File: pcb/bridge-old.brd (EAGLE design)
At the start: 104.2 x 63.6 mm, 38 parts, among them IC2 LM358D, IC3 78L05SMD, X1 PN61729-S

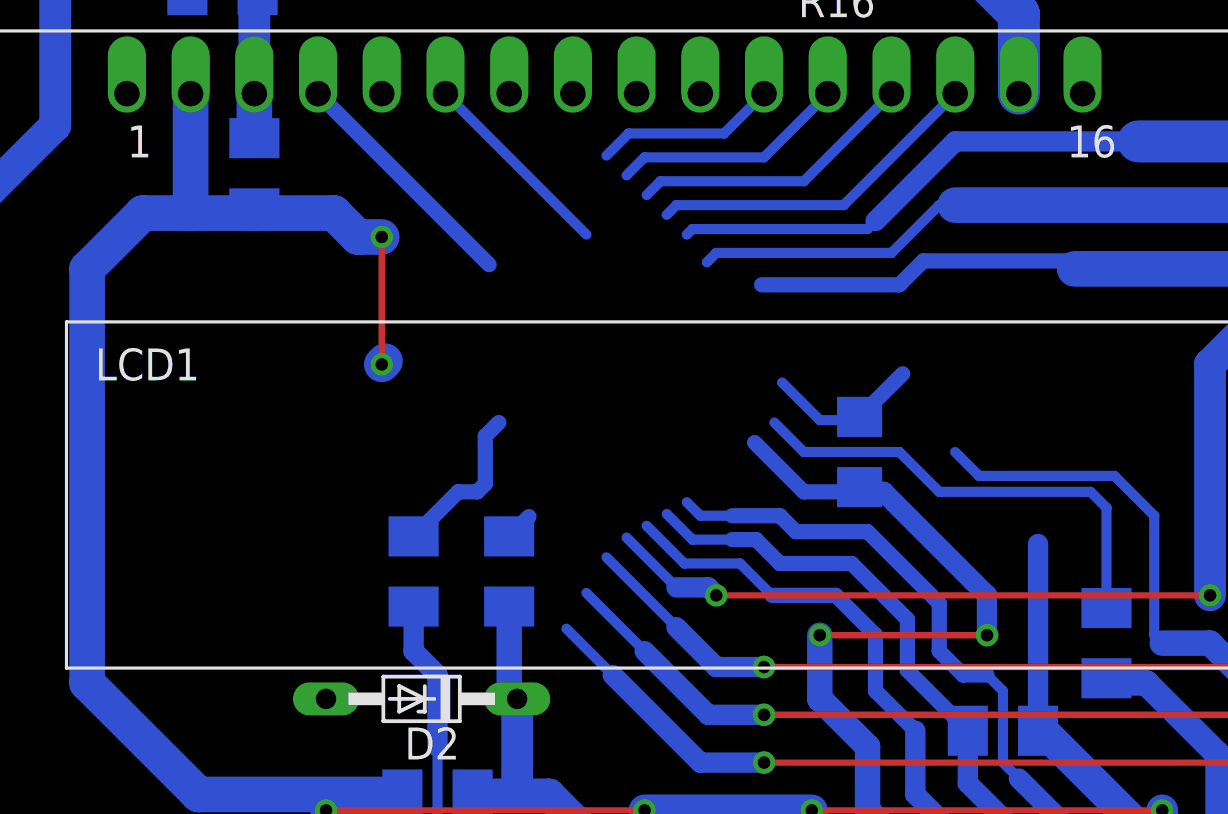
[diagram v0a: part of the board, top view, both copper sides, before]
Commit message: Rename 'bridge' project. Create board for new bridge.
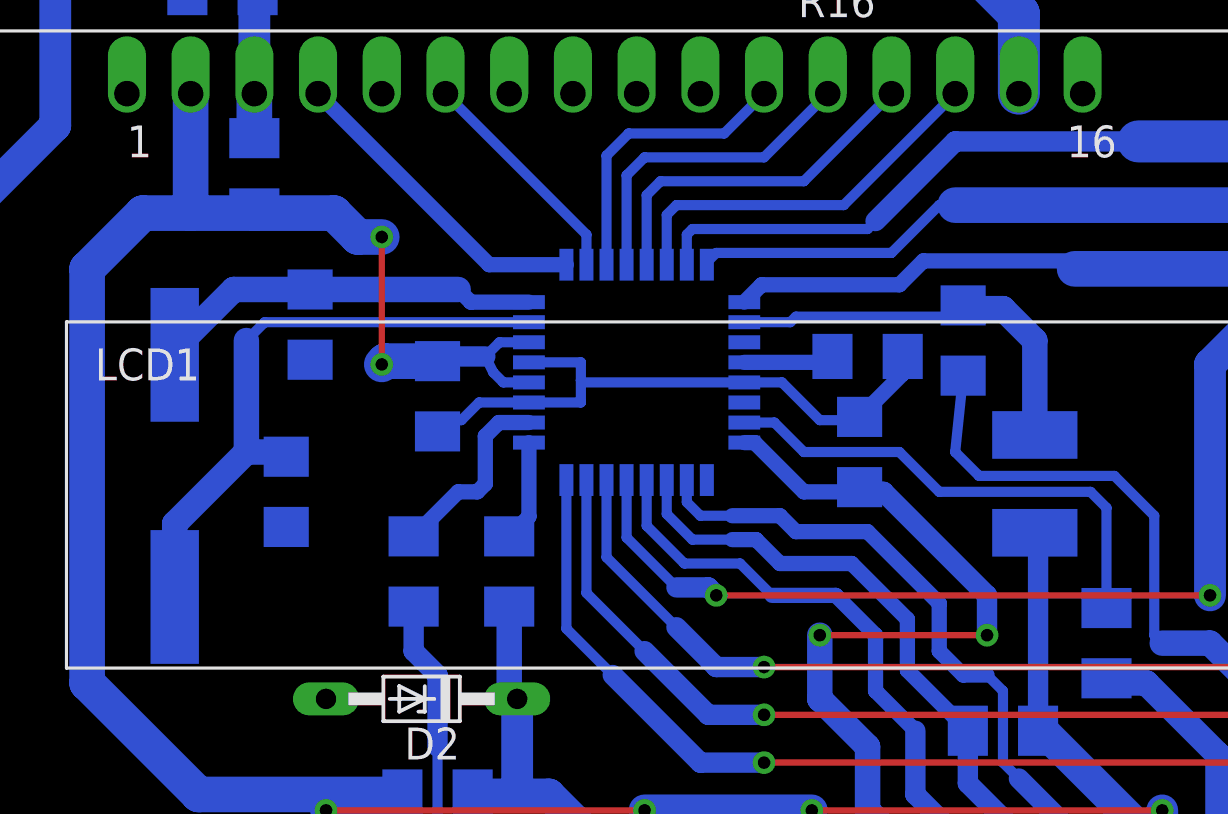
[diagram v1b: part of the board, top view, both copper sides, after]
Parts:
- added C1, C2: 22p, rcl:C1206
- added C3, C4, C5: 100n, rcl:C1206
- added IC1: MEGA8-AI, atmel:TQFP32-08
- added L1: 10u, rcl:L1812
- added Q1: 16MHz, crystal:HC49UP
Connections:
- new net N$10: C4.1, IC1.18, L1.2
- new net N$11: C1.1, IC1.8, Q1.1
- new net N$8: C3.1, IC1.20
- new net N$9: C2.1, IC1.7, Q1.2
- new net PC2: IC1.25
- new net PC6: IC1.19
- new net PC7: IC1.22
- net +5V: now also C5.1, IC1.4, IC1.6, L1.1
- net GND: now also C1.2, C2.2, C3.2, C4.2, C5.2, IC1.21, IC1.3, IC1.5
- net PB0: now also IC1.12
- net PB1: now also IC1.13
- net PB2: now also IC1.14
- net PB3: now also IC1.15
- net PB4: now also IC1.16
- net PB5: now also IC1.17
- net PC0: now also IC1.23
- net PC1: now also IC1.24
- net PC3: now also IC1.26
- net PC4: now also IC1.27
- net PC5: now also IC1.28
- net PD0: now also IC1.30
- net PD1: now also IC1.31
- net PD2: now also IC1.32
- net PD3: now also IC1.1
- net PD4: now also IC1.2
- net PD5: now also IC1.9
- net PD6: now also IC1.10
- net PD7: now also IC1.11
- net RESET: now also IC1.29
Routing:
- net N$9: track 0.00 -> 24.6 mm
- net GND: track 91.7 -> 113.4 mm
- net N$10: track 0.00 -> 16.2 mm
- net N$11: track 0.00 -> 15.6 mm
- net +5V: track 148.3 -> 157.1 mm
- net PD2: track 76.7 -> 82.6 mm
- net PD1: track 69.7 -> 74.2 mm
- net PD7: track 7.30 -> 11.7 mm
- net N$8: track 0.00 -> 3.61 mm
- net PB0: track 9.37 -> 12.9 mm
- net PD5: track 9.64 -> 12.7 mm
- net PD0: track 65.4 -> 68.5 mm
- net PD3: track 1.11 -> 4.06 mm
- net PB1: track 11.4 -> 14.2 mm
- net RESET: track 67.3 -> 69.6 mm
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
